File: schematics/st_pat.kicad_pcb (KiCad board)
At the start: 2 copper layers, 121.9 x 87 mm, 19 parts, among them J4 BATTERY, SW1 SW_PWR, SW2 BTN_RST, SW3 BTN, SW4 BTN, SW5 BTN, U1 GPS_Breakout_746, U2 FEATHER_M0_BASIC_PROTO, U3 LIS2MDL_ADAFRUIT, U4 Sharp_Display_4694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

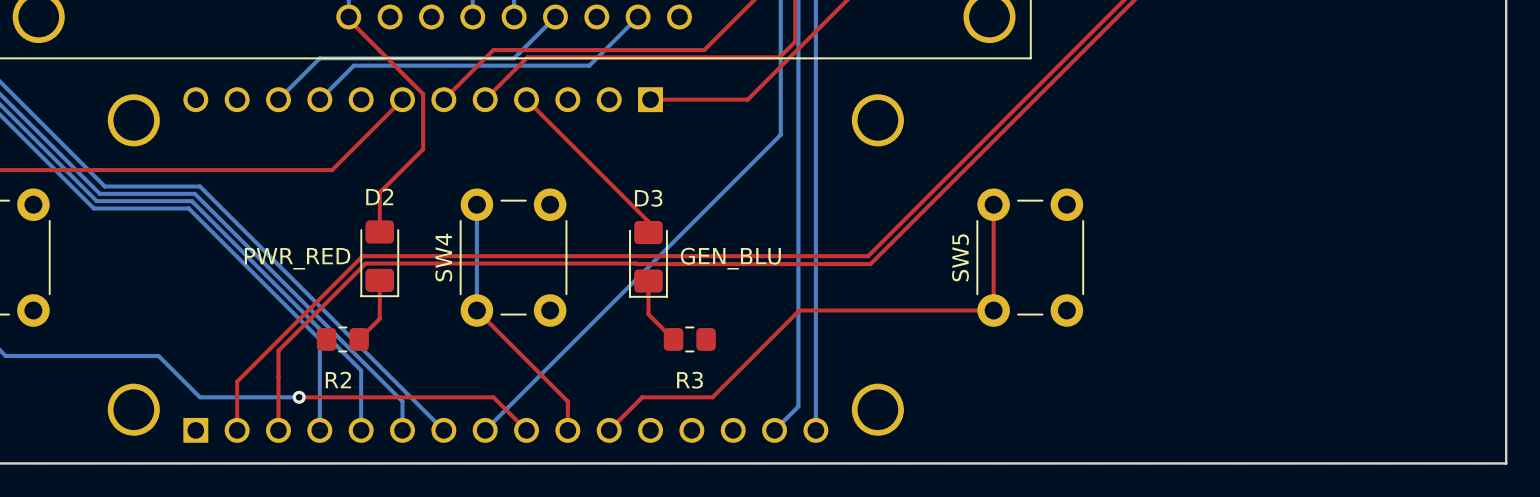
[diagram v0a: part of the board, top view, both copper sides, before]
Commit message: increase spacing for leds
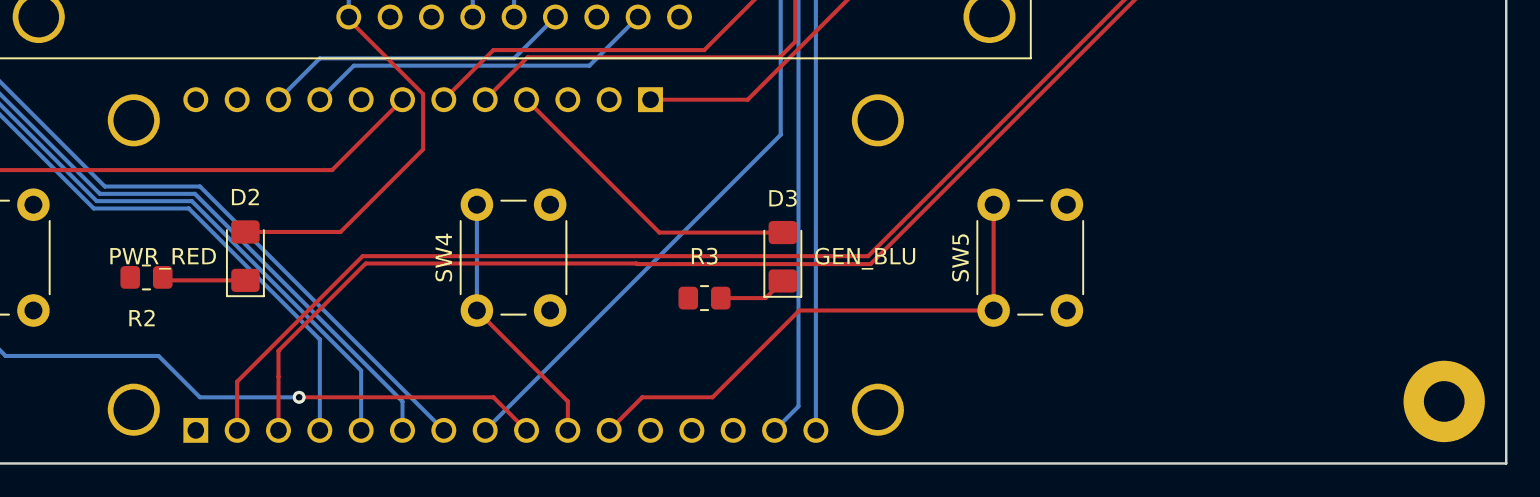
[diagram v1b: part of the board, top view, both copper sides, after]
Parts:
- added  : , MountingHole:MountingHole_2.5mm_Pad, F.Cu at (196.8, 120.7)
- moved R2 12.7 mm to (117.1, 113.0)
- moved D2 8.25 mm to (123.2, 111.7)
- moved D3 8.25 mm to (156.2, 111.8)
- moved R3 2.70 mm to (151.4, 114.3), turned to 180 degrees
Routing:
- net Net-(D3-Pad2): track 11.3 -> 19.1 mm
- net +3V3: track 244.3 -> 251.2 mm
- net Net-(D2-Pad1): track 4.16 -> 5.15 mm
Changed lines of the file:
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@@
     (tracks 189)
     (zones 0)
-    (modules 19)
+    (modules 20)
     (nets 24)
   )
@@
     (add_net "Net-(J4-Pad1)")
   )
+  (module MountingHole:MountingHole_2.5mm_Pad (layer F.Cu)
+    (at 196.85 120.65)
+    (descr "Mounting Hole 2.5mm")
+    (tags "mounting hole 2.5mm")
+    (attr virtual)
+    (fp_text reference " " (at 0 -0.254) (layer F.SilkS)
+      (effects (font (size 1 1) (thickness 0.15)))
+    )
+    (fp_text value " " (at 0 -0.254) (layer F.Fab)
+      (effects (font (size 1 1) (thickness 0.15)))
+    )
+    (fp_circle (center 0 0) (end 2.5 0) (layer Cmts.User) (width 0.15))
+    (fp_circle (center 0 0) (end 2.75 0) (layer F.CrtYd) (width 0.05))
+    (fp_text user %R (at 0.3 0) (layer F.Fab)
+      (effects (font (size 1 1) (thickness 0.15)))
+    )
+    (pad 1 thru_hole circle (at 0 0) (size 5 5) (drill 2.5) (layers *.Cu *.Mask))
+  )
   (module st_pat:GPS_Breakout_746 (layer F.Cu)
     (at 185.42 97.028 180)
@@
   )
   (module Resistor_SMD:R_0805_2012Metric_Pad1.20x1.40mm_HandSolder (layer F.Cu)
-    (at 150.495 116.84)
+    (at 151.4 114.3 180)
     (descr "Resistor SMD 0805 (2012 Metric), square (rectangular) end terminal, IPC_7351 nominal with elongated pad for handsoldering. (Body size source: IPC-SM-782 page 72, https://www.pcb-3d.com/wordpress/wp-content/uploads/ipc-sm-782a_amendment_1_and_2.pdf), generated with kicad-footprint-generator")
     (tags "resistor handsolder")
@@
       (effects (font (size 0.5 0.5) (thickness 0.08)))
     )
-    (pad 2 smd roundrect (at 1 0) (size 1.2 1.4) (layers F.Cu F.Paste F.Mask) (roundrect_rratio 0.2083325)
-      (net 1 GND))
-    (pad 1 smd roundrect (at -1 0) (size 1.2 1.4) (layers F.Cu F.Paste F.Mask) (roundrect_rratio 0.2083325)
+    (pad 2 smd roundrect (at 1 0 180) (size 1.2 1.4) (layers F.Cu F.Paste F.Mask) (roundrect_rratio 0.2083325)
+      (net 1 GND))
+    (pad 1 smd roundrect (at -1 0 180) (size 1.2 1.4) (layers F.Cu F.Paste F.Mask) (roundrect_rratio 0.2083325)
       (net 18 "Net-(D3-Pad1)"))
     (model ${KISYS3DMOD}/Resistor_SMD.3dshapes/R_0805_2012Metric.wrl
@@
   )
   (module LED_SMD:LED_1206_3216Metric_Pad1.42x1.75mm_HandSolder (layer F.Cu)
-    (at 147.955 111.76 90)
+    (at 156.21 111.76 90)
     (descr "LED SMD 1206 (3216 Metric), square (rectangular) end terminal, IPC_7351 nominal, (Body size source: http://www.tortai-tech.com/upload/download/2011102023233369053.pdf), generated with kicad-footprint-generator")
     (tags "LED handsolder")
@@
   )
   (module Resistor_SMD:R_0805_2012Metric_Pad1.20x1.40mm_HandSolder (layer F.Cu)
-    (at 129.175 116.84 180)
+    (at 117.11 113.03 180)
     (descr "Resistor SMD 0805 (2012 Metric), square (rectangular) end terminal, IPC_7351 nominal with elongated pad for handsoldering. (Body size source: IPC-SM-782 page 72, https://www.pcb-3d.com/wordpress/wp-content/uploads/ipc-sm-782a_amendment_1_and_2.pdf), generated with kicad-footprint-generator")
     (tags "resistor handsolder")
@@
   )
   (module LED_SMD:LED_1206_3216Metric_Pad1.42x1.75mm_HandSolder (layer F.Cu)
-    (at 131.445 111.7235 90)
+    (at 123.19 111.7235 90)
     (descr "LED SMD 1206 (3216 Metric), square (rectangular) end terminal, IPC_7351 nominal, (Body size source: http://www.tortai-tech.com/upload/download/2011102023233369053.pdf), generated with kicad-footprint-generator")
     (tags "LED handsolder")
@@
   (segment (start 142.748 69.088) (end 121.412 69.088) (width 0.25) (layer B.Cu) (net 2))
   (segment (start 154.432 69.088) (end 142.748 69.088) (width 0.25) (layer B.Cu) (net 2))
-  (segment (start 131.445 110.236) (end 131.445 107.823) (width 0.25) (layer F.Cu) (net 2))
-  (segment (start 131.445 107.823) (end 134.112 105.156) (width 0.25) (layer F.Cu) (net 2))
   (segment (start 129.54 97.192798) (end 129.54 97.028) (width 0.25) (layer F.Cu) (net 2))
   (segment (start 134.112 101.764798) (end 129.54 97.192798) (width 0.25) (layer F.Cu) (net 2))
   (segment (start 134.112 105.156) (end 134.112 101.764798) (width 0.25) (layer F.Cu) (net 2))
+  (segment (start 129.032 110.236) (end 134.112 105.156) (width 0.25) (layer F.Cu) (net 2))
+  (segment (start 123.19 110.236) (end 129.032 110.236) (width 0.25) (layer F.Cu) (net 2))
   (segment (start 174.752 59.436) (end 185.42 59.436) (width 0.25) (layer F.Cu) (net 3))
   (segment (start 151.384 99.06) (end 155.956 94.488) (width 0.25) (layer F.Cu) (net 3))
@@
   (segment (start 135.382 102.108) (end 138.43 99.06) (width 0.25) (layer F.Cu) (net 3))
   (segment (start 139.192 99.06) (end 151.384 99.06) (width 0.25) (layer F.Cu) (net 3))
-  (segment (start 130.175 116.84) (end 131.445 115.57) (width 0.25) (layer F.Cu) (net 4))
-  (segment (start 131.445 115.57) (end 131.445 113.211) (width 0.25) (layer F.Cu) (net 4))
+  (segment (start 118.291 113.211) (end 118.11 113.03) (width 0.25) (layer F.Cu) (net 4))
+  (segment (start 123.19 113.211) (end 118.291 113.211) (width 0.25) (layer F.Cu) (net 4))
   (segment (start 158.623 122.047) (end 158.242 122.428) (width 0.25) (layer B.Cu) (net 5))
   (segment (start 158.242 122.428) (end 158.242 75.946) (width 0.25) (layer B.Cu) (net 5))
@@
   (segment (start 184.912 47.752) (end 178.435 41.275) (width 0.25) (layer F.Cu) (net 16))
   (segment (start 184.912 52.832) (end 184.912 47.752) (width 0.25) (layer F.Cu) (net 16))
-  (segment (start 147.955 109.601) (end 147.955 110.2725) (width 0.25) (layer F.Cu) (net 17))
-  (segment (start 140.462 102.108) (end 147.955 109.601) (width 0.25) (layer F.Cu) (net 17))
-  (segment (start 147.955 115.3) (end 149.495 116.84) (width 0.25) (layer F.Cu) (net 18))
-  (segment (start 147.955 113.2475) (end 147.955 115.3) (width 0.25) (layer F.Cu) (net 18))
+  (segment (start 148.6265 110.2725) (end 156.21 110.2725) (width 0.25) (layer F.Cu) (net 17))
+  (segment (start 140.462 102.108) (end 148.6265 110.2725) (width 0.25) (layer F.Cu) (net 17))
+  (segment (start 155.1575 114.3) (end 156.21 113.2475) (width 0.25) (layer F.Cu) (net 18))
+  (segment (start 152.4 114.3) (end 155.1575 114.3) (width 0.25) (layer F.Cu) (net 18))
   (segment (start 116.84 71.882) (end 116.713 71.755) (width 0.25) (layer B.Cu) (net 19))
   (segment (start 116.84 84.836) (end 116.84 71.882) (width 0.25) (layer B.Cu) (net 19))

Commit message: add waterloo rocketry logo and generate gerber
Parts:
- added G***: LOGO, st_pat:Logo_SilkScreen_10mm, B.Cu at (185.4, 107.7)
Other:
- board text added: "St Pats Rio Liu Waterloo Rocketry 2021-09-29"
